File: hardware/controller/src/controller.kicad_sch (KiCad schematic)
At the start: 31 parts, among them J1 To Display, J2 Display, J3 Barrel_Jack_Switch, J4 Program, J5 JTAG, SW1 RESET, SW2 BTN1, SW3 BTN1, U1 ESP32-WROOM-32D, U2 XL1509-5.0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

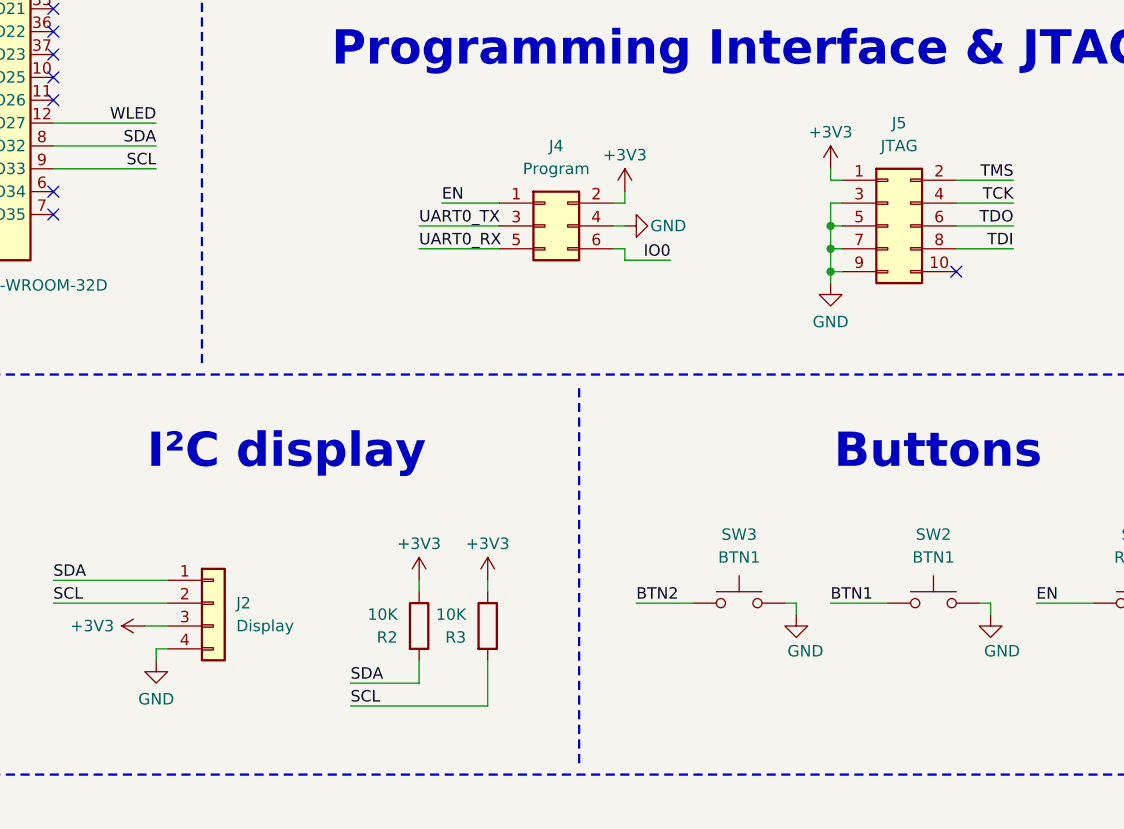
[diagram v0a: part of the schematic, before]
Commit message: Added TVS diode to UART line on side pannel
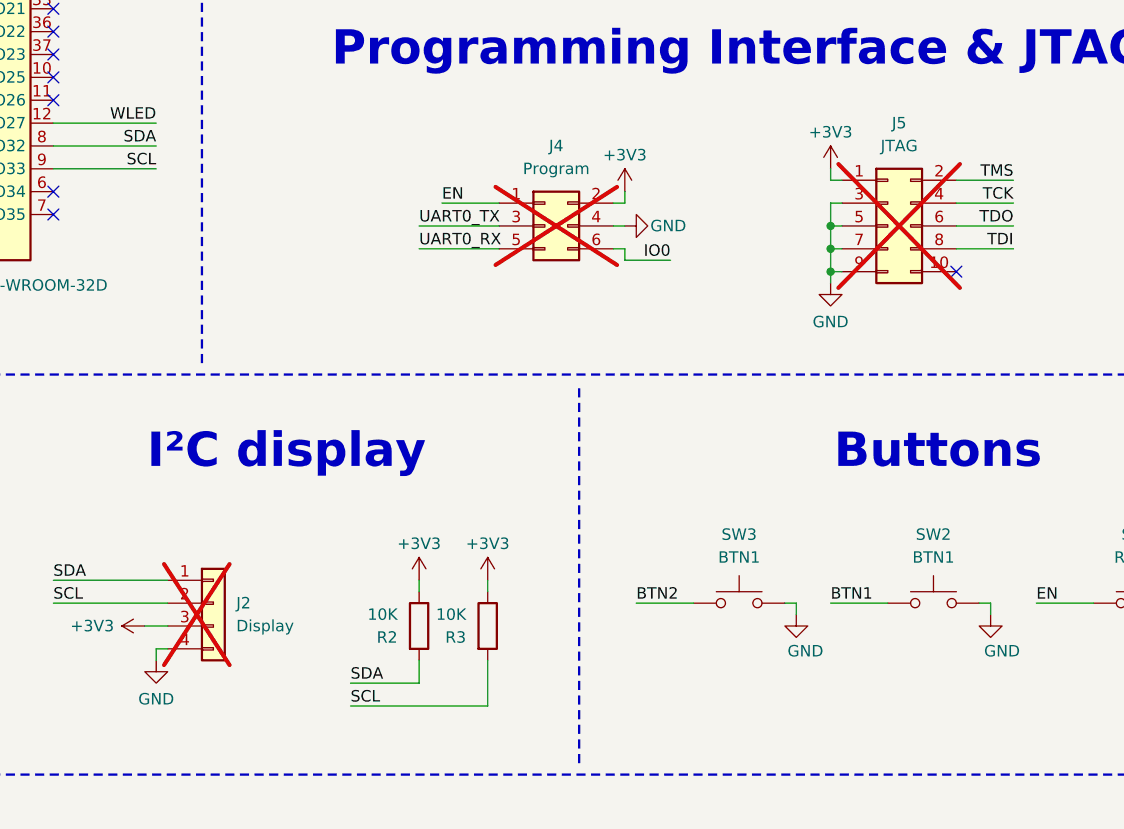
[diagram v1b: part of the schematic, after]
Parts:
- D3: LCSC (none) -> C2761795
- J1: LCSC (none) -> C3406
- J2, J4, J5: now not fitted
- J3: LCSC (none) -> C319133
- L2: LCSC C53663 -> C36414
- SW1, SW2, SW3: LCSC (none) -> C5340120
- U1: LCSC (none) -> C529578
- U4: LCSC (none) -> C1509088,C783414
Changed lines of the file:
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@@
 		(in_bom yes)
 		(on_board yes)
-		(dnp no)
+		(dnp yes)
 		(fields_autoplaced yes)
 		(property "Reference" "J4"
@@
 		(in_bom yes)
 		(on_board yes)
-		(dnp no)
+		(dnp yes)
 		(fields_autoplaced yes)
 		(property "Reference" "J2"
@@
 			)
 		)
+		(property "LCSC" "C5340120"
+			(at 139.7 146.05 0)
+			(effects
+				(font
+					(size 1.27 1.27)
+				)
+				(hide yes)
+			)
+		)
 		(pin "1"
 		)
@@
 			)
 		)
+		(property "LCSC" "C2761795"
+			(at 34.29 148.59 0)
+			(effects
+				(font
+					(size 1.27 1.27)
+				)
+				(hide yes)
+			)
+		)
 		(pin "4"
 		)
@@
 			)
 		)
+		(property "LCSC" "C529578"
+			(at 48.26 74.93 0)
+			(effects
+				(font
+					(size 1.27 1.27)
+				)
+				(hide yes)
+			)
+		)
 		(pin "25"
 		)
@@
 			)
 		)
+		(property "LCSC" "C5340120"
+			(at 161.29 146.05 0)
+			(effects
+				(font
+					(size 1.27 1.27)
+				)
+				(hide yes)
+			)
+		)
 		(pin "1"
 		)
@@
 			)
 		)
+		(property "LCSC" "C1509088,C783414"
+			(at 106.68 52.07 0)
+			(effects
+				(font
+					(size 1.27 1.27)
+				)
+				(hide yes)
+			)
+		)
 		(pin "4"
 		)
@@
 			)
 		)
-		(property "LCSC" "C53663"
+		(property "LCSC" " C36414"
 			(at 81.28 203.2 90)
 			(effects
@@
 			)
 		)
+		(property "LCSC" "C5340120"
+			(at 184.15 146.05 0)
+			(effects
+				(font
+					(size 1.27 1.27)
+				)
+				(hide yes)
+			)
+		)
 		(pin "1"
 		)
@@
 		(in_bom yes)
 		(on_board yes)
-		(dnp no)
+		(dnp yes)
 		(fields_autoplaced yes)
 		(property "Reference" "J5"
@@
 			)
 		)
+		(property "LCSC" "C3406"
+			(at 163.83 50.8 0)
+			(effects
+				(font
+					(size 1.27 1.27)
+				)
+				(hide yes)
+			)
+		)
 		(pin "11"
 		)
@@
 			(at 31.75 181.61 0)
 			(effects
+				(font
+					(size 1.27 1.27)
+				)
+				(hide yes)
+			)
+		)
+		(property "LCSC" "C319133"
+			(at 31.75 181.61 0)
+			(effects

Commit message: Fix CI ERC & DRC errors
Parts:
- L2: LCSC C36414 -> C36414
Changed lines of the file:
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@@
 			)
 		)
-		(property "LCSC" " C36414"
+		(property "LCSC" "C36414"
 			(at 81.28 203.2 90)
 			(effects

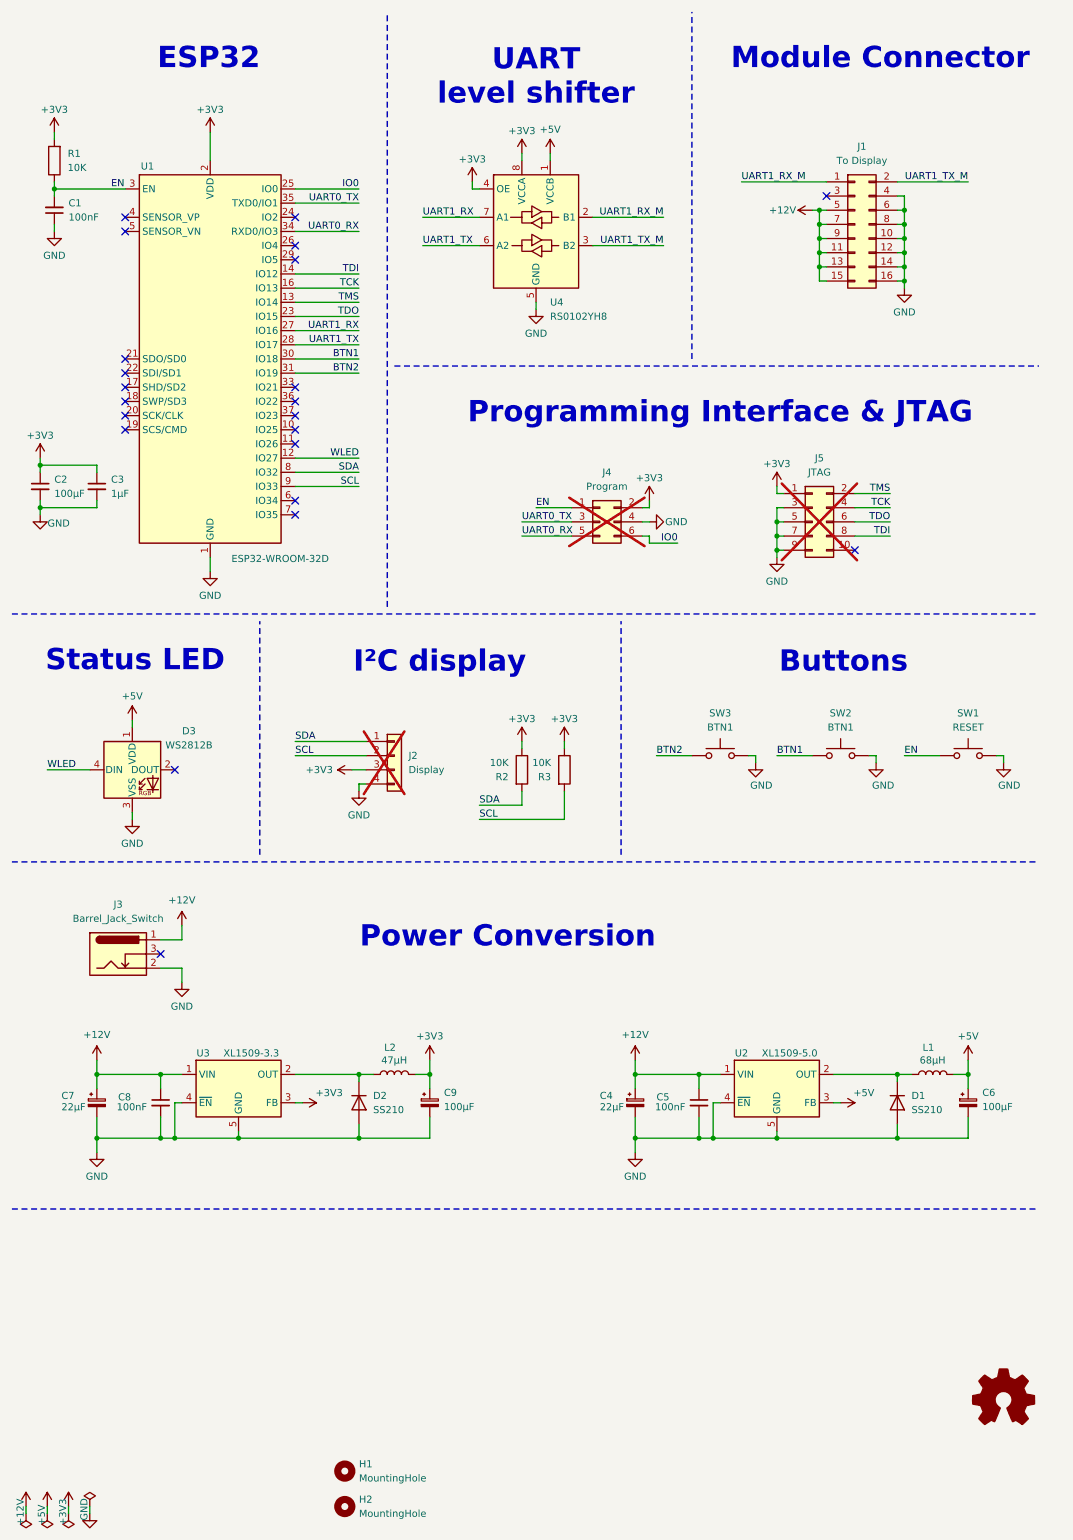
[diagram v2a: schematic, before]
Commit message: Changed micro symbol to uF
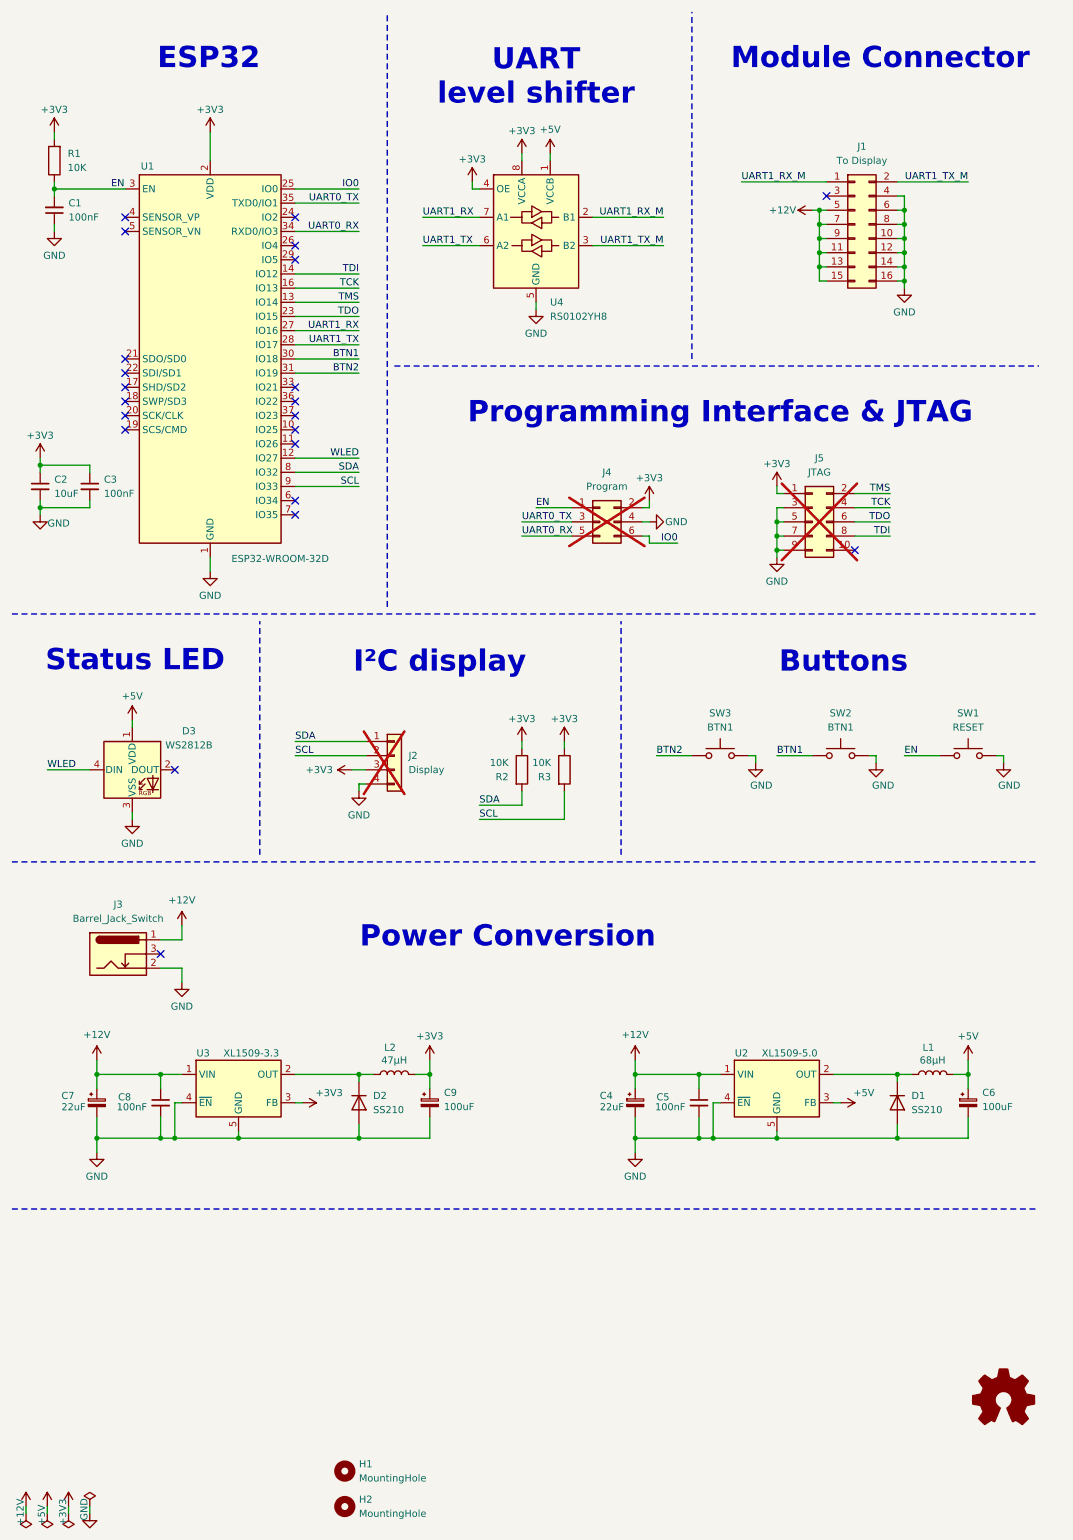
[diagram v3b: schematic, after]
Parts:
- C2: value 100µF -> 10uF
- C3: value 1µF -> 100nF
- C4, C7: value 22µF -> 22uF
- C6, C9: value 100µF -> 100uF
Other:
- moved on the sheet: C3
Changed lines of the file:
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@@
 	(wire
 		(pts
-			(xy 27.94 100.33) (xy 27.94 101.6)
+			(xy 26.67 100.33) (xy 26.67 101.6)
 		)
 		(stroke
@@
 	(wire
 		(pts
-			(xy 17.78 93.98) (xy 27.94 93.98)
+			(xy 17.78 93.98) (xy 26.67 93.98)
 		)
 		(stroke
@@
 	(wire
 		(pts
-			(xy 17.78 101.6) (xy 27.94 101.6)
+			(xy 17.78 101.6) (xy 26.67 101.6)
 		)
 		(stroke
@@
 	(wire
 		(pts
-			(xy 27.94 93.98) (xy 27.94 95.25)
+			(xy 26.67 93.98) (xy 26.67 95.25)
 		)
 		(stroke
@@
 			)
 		)
-		(property "Value" "100µF"
+		(property "Value" "100uF"
 			(at 186.69 209.0039 0)
 			(effects
@@
 			)
 		)
-		(property "Value" "100µF"
+		(property "Value" "100uF"
 			(at 90.17 209.0039 0)
 			(effects
@@
 			)
 		)
-		(property "Value" "22µF"
+		(property "Value" "22uF"
 			(at 118.11 209.042 0)
 			(effects
@@
 	(symbol
 		(lib_id "Device:C_Small")
-		(at 27.94 97.79 0)
+		(at 26.67 97.79 0)
 		(unit 1)
 		(exclude_from_sim no)
@@
 		(fields_autoplaced yes)
 		(property "Reference" "C3"
-			(at 30.48 96.5263 0)
+			(at 29.21 96.5263 0)
 			(effects
 				(font
@@
 			)
 		)
-		(property "Value" "1µF"
-			(at 30.48 99.0663 0)
+		(property "Value" "100nF"
+			(at 29.21 99.0663 0)
 			(effects
 				(font
@@
 		)
 		(property "Footprint" "Capacitor_SMD:C_0805_2012Metric"
-			(at 27.94 97.79 0)
+			(at 26.67 97.79 0)
 			(effects
 				(font
@@
 		)
 		(property "Datasheet" "~"
-			(at 27.94 97.79 0)
+			(at 26.67 97.79 0)
 			(effects
 				(font
@@
 		)
 		(property "Description" "Unpolarized capacitor, small symbol"
-			(at 27.94 97.79 0)
+			(at 26.67 97.79 0)
 			(effects
 				(font
@@
 			)
 		)
-		(property "Value" "100µF"
+		(property "Value" "10uF"
 			(at 20.32 99.0663 0)
 			(effects
@@
 			)
 		)
-		(property "Value" "22µF"
+		(property "Value" "22uF"
 			(at 21.59 209.042 0)
 			(effects

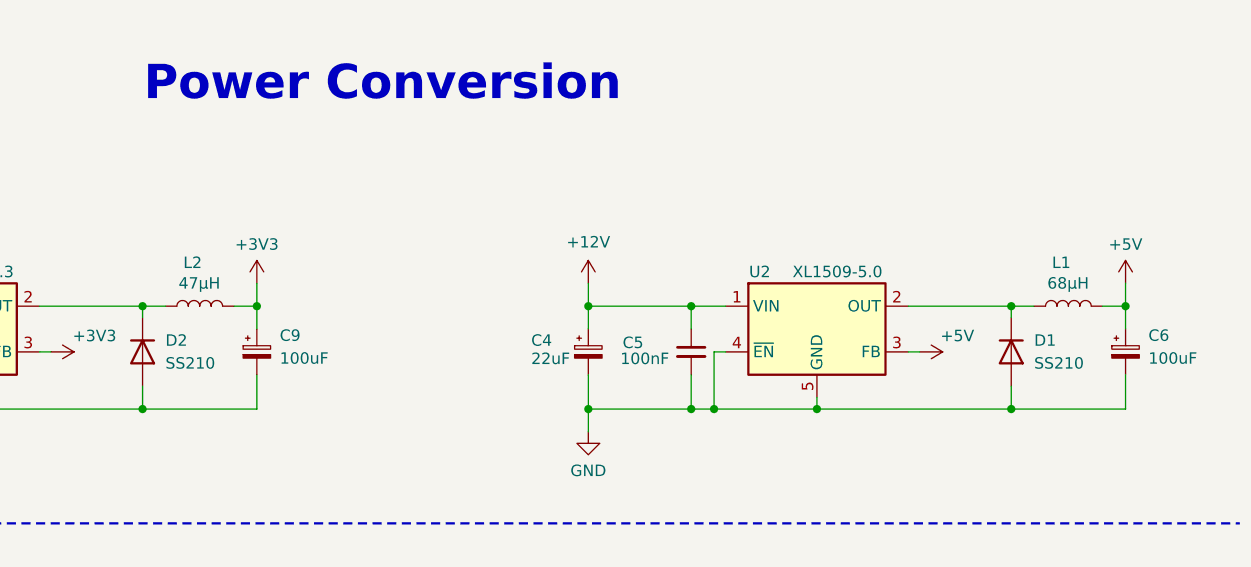
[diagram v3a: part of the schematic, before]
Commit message: Changed micro symbol to uF
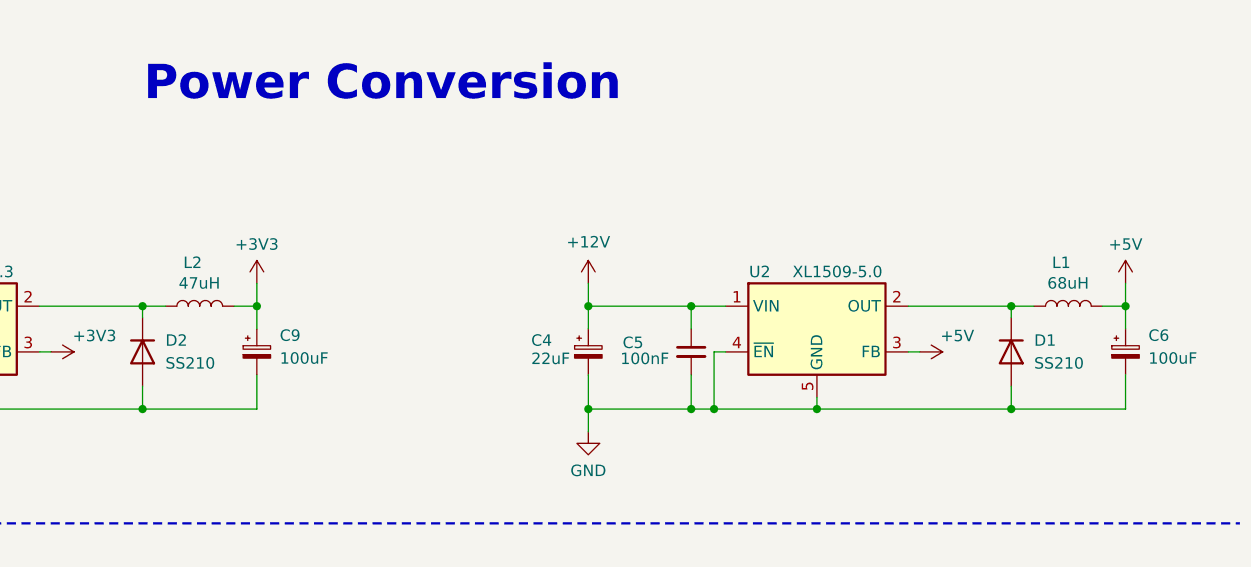
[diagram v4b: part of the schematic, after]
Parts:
- L1: value 68µH -> 68uH
- L2: value 47µH -> 47uH
- U3: LCSC C61063 -> C2681226
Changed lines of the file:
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@@
 			)
 		)
-		(property "LCSC" "C61063"
+		(property "LCSC" "C2681226"
 			(at 53.34 205.74 0)
 			(effects
@@
 			)
 		)
-		(property "Value" "47µH"
+		(property "Value" "47uH"
 			(at 83.566 200.66 90)
 			(effects
@@
 			)
 		)
-		(property "Value" "68µH"
+		(property "Value" "68uH"
 			(at 180.086 200.66 90)
 			(effects
